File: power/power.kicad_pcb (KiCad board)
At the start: 0 parts

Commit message: mainboard v0.3 + power WIP
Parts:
- added BT1: Cell 1, Connector_PinHeader_2.54mm:PinHeader_1x02_P2.54mm_Vertical, F.Cu at (70.8, 190.2)
- added BT2: Cell 2, Connector_PinHeader_2.54mm:PinHeader_1x02_P2.54mm_Vertical, F.Cu at (70.8, 196.4)
- added BT3: Cell 3, Connector_PinHeader_2.54mm:PinHeader_1x02_P2.54mm_Vertical, F.Cu at (70.8, 202.6)
- added BT4: Cell 4, Connector_PinHeader_2.54mm:PinHeader_1x02_P2.54mm_Vertical, F.Cu at (70.8, 208.8)
- added C1: 1uF, Capacitor_SMD:C_0603_1608Metric, F.Cu at (187.0, 118.2)
- added C10: 100nF, Capacitor_SMD:C_0603_1608Metric, F.Cu at (184.8, 107.3)
- added C11: 1uF, Capacitor_SMD:C_0603_1608Metric, F.Cu at (57.8, 164.6)
- added C12: 1uF, Capacitor_SMD:C_0603_1608Metric, F.Cu at (57.8, 167.1)
- added C13: 1uF, Capacitor_SMD:C_0603_1608Metric, F.Cu at (75.1, 191.7)
- added C14: 1uF, Capacitor_SMD:C_0603_1608Metric, F.Cu at (75.2, 196.6)
- added C15: 1uF, Capacitor_SMD:C_0603_1608Metric, F.Cu at (75.1, 202.0)
- added C16: 1uF, Capacitor_SMD:C_0603_1608Metric, F.Cu at (75.2, 208.1)
- added C17: 1uF, Capacitor_SMD:C_0603_1608Metric, F.Cu at (75.3, 211.7)
- added C18: 0.1uF, Capacitor_SMD:C_0603_1608Metric, F.Cu at (100.0, 187.0)
- added C19: 0.1uF, Capacitor_SMD:C_0603_1608Metric, F.Cu at (100.0, 189.6)
- added C2: 10uF, Capacitor_SMD:C_0603_1608Metric, F.Cu at (36.5, 64.1)
- added C20: 0.1uF, Capacitor_SMD:C_0603_1608Metric, F.Cu at (100.0, 192.1)
- added C21: 0.1uF, Capacitor_SMD:C_0603_1608Metric, F.Cu at (100.0, 194.6)
- added C22: 0.1uF, Capacitor_SMD:C_0603_1608Metric, F.Cu at (104.0, 187.0)
- added C23: 1uF, Capacitor_SMD:C_0603_1608Metric, F.Cu at (73.6, 208.1)
- added C24: 10uF, Capacitor_SMD:C_0603_1608Metric, F.Cu at (69.8, 186.7)
- added C25: 10uF, Capacitor_SMD:C_0603_1608Metric, F.Cu at (71.4, 186.7)
- added C26: 100nF, Capacitor_SMD:C_0603_1608Metric, F.Cu at (73.1, 186.7)
- added C27: 1uF, Capacitor_SMD:C_0603_1608Metric, F.Cu at (174.4, 112.8)
- added C28: 10uF, Capacitor_SMD:C_0603_1608Metric, F.Cu at (181.6, 107.4)
- added C29: 10uF, Capacitor_SMD:C_0603_1608Metric, F.Cu at (186.4, 107.3)
- added C3: 10uF, Capacitor_SMD:C_0603_1608Metric, F.Cu at (36.5, 66.6)
- added C30: 10uF, Capacitor_SMD:C_0603_1608Metric, F.Cu at (182.8, 110.6)
- added C31: 10uF, Capacitor_SMD:C_0603_1608Metric, F.Cu at (181.1, 112.8)
- added C32: 10uF, Capacitor_SMD:C_0603_1608Metric, F.Cu at (179.4, 112.8)
- added C33: 10uF, Capacitor_SMD:C_0603_1608Metric, F.Cu at (177.8, 112.8)
- added C34: 33nF, Capacitor_SMD:C_0603_1608Metric, F.Cu at (178.5, 105.4)
- added C35: 33nF, Capacitor_SMD:C_0603_1608Metric, F.Cu at (172.9, 105.4)
- added C36: 470nF, Capacitor_SMD:C_0603_1608Metric, F.Cu at (162.8, 107.6)
- added C37: 10nF, Capacitor_SMD:C_0603_1608Metric, F.Cu at (172.7, 112.8)
- added C38: 47nF, Capacitor_SMD:C_0603_1608Metric, F.Cu at (161.9, 110.5)
- added C39: 47nF, Capacitor_SMD:C_0603_1608Metric, F.Cu at (155.6, 110.5)
- added C4: 10uF, Capacitor_SMD:C_0603_1608Metric, F.Cu at (36.5, 69.1)
- added C40: 10uF, Capacitor_SMD:C_0603_1608Metric, F.Cu at (145.2, 107.6)
- added C41: 10uF, Capacitor_SMD:C_0603_1608Metric, F.Cu at (143.4, 107.6)
- added C42: 10uF, Capacitor_SMD:C_0603_1608Metric, F.Cu at (141.6, 107.6)
- added C43: 10uF, Capacitor_SMD:C_0603_1608Metric, F.Cu at (141.8, 104.4)
- added C44: 10uF, Capacitor_SMD:C_0603_1608Metric, F.Cu at (143.5, 104.4)
- added C45: 10uF, Capacitor_SMD:C_0603_1608Metric, F.Cu at (145.3, 104.4)
- added C46: 1uF, Capacitor_SMD:C_0603_1608Metric, F.Cu at (145.2, 95.2)
- added C47: 2.2uF, Capacitor_SMD:C_0603_1608Metric, F.Cu at (158.8, 110.5)
- added C48: 1uF, Capacitor_SMD:C_0603_1608Metric, F.Cu at (163.8, 105.0)
- added C49: 680pF, Capacitor_SMD:C_0603_1608Metric, F.Cu at (153.5, 99.2)
- added C5: 0.1uF, Capacitor_SMD:C_0603_1608Metric, F.Cu at (36.5, 71.6)
- added C50: 15pF, Capacitor_SMD:C_0603_1608Metric, F.Cu at (154.3, 101.6)
- added C51: 33pF, Capacitor_SMD:C_0603_1608Metric, F.Cu at (157.5, 101.5)
- added C52: 1800pF, Capacitor_SMD:C_0603_1608Metric, F.Cu at (156.7, 99.2)
- added C53: 100pF, Capacitor_SMD:C_0603_1608Metric, F.Cu at (163.9, 103.3)
- added C54: 100pF, Capacitor_SMD:C_0603_1608Metric, F.Cu at (164.7, 100.8)
- added C55: 0.1uF, Capacitor_SMD:C_0603_1608Metric, F.Cu at (142.0, 96.0)
- added C56: 10uF, Capacitor_SMD:C_0603_1608Metric, F.Cu at (126.4, 16.2)
- added C57: 0.1uF, Resistor_SMD:R_0603_1608Metric, F.Cu at (126.4, 18.7)
- added C6: 1uF, Capacitor_SMD:C_0603_1608Metric, F.Cu at (126.4, 11.2)
- added C7: 1uF, Capacitor_SMD:C_0603_1608Metric, F.Cu at (126.4, 13.7)
- added C8: 10uF, Capacitor_SMD:C_0603_1608Metric, F.Cu at (183.2, 107.4)
- added C9: 10uF, Capacitor_SMD:C_0603_1608Metric, F.Cu at (184.5, 110.5)
- added D1: MMSZ5248B, Diode_SMD:D_SOD-123, F.Cu at (100.9, 206.9)
- added D2: BAS316, Diode_SMD:D_SOD-323, F.Cu at (78.0, 182.2)
- added D3: SMBJ26A-13-F, Diode_SMD:D_SMB, F.Cu at (77.8, 186.0)
- added D4: LED1, LED_SMD:LED_0603_1608Metric, F.Cu at (121.8, 36.6)
- added D5: LED2, LED_SMD:LED_0603_1608Metric, F.Cu at (121.8, 39.2)
- added D6: LED3, LED_SMD:LED_0603_1608Metric, F.Cu at (121.8, 41.8)
- added D7: LED4, LED_SMD:LED_0603_1608Metric, F.Cu at (121.8, 44.4)
- added D8: LED5, LED_SMD:LED_0603_1608Metric, F.Cu at (121.8, 46.9)
- added J1: USB-C Power + USB2.0, Connector_USB:USB_C_Receptacle_HRO_TYPE-C-31-M-12, F.Cu at (196.9, 113.1)
- added J2: USB, FPC:FPC-SMD_6P-P0.50_XUNPU_FPC-05F-6PH20, F.Cu at (103.2, 130.6)
- added L1: MWSA0603S-100MT, Inductor_SMD:L_Sunlord_MWSA0603S, F.Cu at (43.4, 67.0)
- added L2: MWSA0603S-2R2MT, Inductor_SMD:L_Sunlord_MWSA0603S, F.Cu at (158.7, 115.2)
- added Q1: SI7617DN-T1-GE3, Package_SO:Vishay_PowerPAK_1212-8_Single, F.Cu at (187.9, 110.9)
- added Q2: CSD18534Q5A, Package_TO_SOT_SMD:TDSON-8-1, F.Cu at (111.7, 199.2)
- added Q3: CSD18534Q5A, Package_TO_SOT_SMD:TDSON-8-1, F.Cu at (111.7, 205.9)
- added Q4: CSD18534Q5A, Package_TO_SOT_SMD:TDSON-8-1, F.Cu at (168.6, 108.7)
- added Q5: CSD18534Q5A, Package_TO_SOT_SMD:TDSON-8-1, F.Cu at (168.1, 115.5)
- added Q6: CSD18534Q5A, Package_TO_SOT_SMD:TDSON-8-1, F.Cu at (149.3, 115.6)
- added Q7: CSD18534Q5A, Package_TO_SOT_SMD:TDSON-8-1, F.Cu at (149.7, 108.5)
- added Q8: CSD18534Q5A, Package_TO_SOT_SMD:TDSON-8-1, F.Cu at (149.7, 100.8)
- added R1: 1M, Resistor_SMD:R_0603_1608Metric, F.Cu at (193.1, 106.8)
- added R10: 33R, Resistor_SMD:R_0603_1608Metric, F.Cu at (74.3, 189.3)
- added R11: 7.5k, Resistor_SMD:R_0603_1608Metric, F.Cu at (36.5, 74.1)
- added R12: 24k, Resistor_SMD:R_0603_1608Metric, F.Cu at (36.5, 76.7)
- added R13: 56k, Resistor_SMD:R_0603_1608Metric, F.Cu at (36.5, 79.2)
- added R14: 10k, Resistor_SMD:R_0603_1608Metric, F.Cu at (36.5, 81.7)
- added R15: 33R, Resistor_SMD:R_0603_1608Metric, F.Cu at (74.4, 194.2)
- added R16: 33R, Resistor_SMD:R_0603_1608Metric, F.Cu at (74.4, 199.4)
- added R17: 33R, Resistor_SMD:R_0603_1608Metric, F.Cu at (74.4, 204.9)
- added R18: 33R, Resistor_SMD:R_0603_1608Metric, F.Cu at (73.7, 211.7)
- added R19: 1k, Resistor_SMD:R_0603_1608Metric, F.Cu at (65.8, 172.2)
- added R2: 10R, Resistor_SMD:R_0603_1608Metric, F.Cu at (190.1, 118.2)
- added R20: 15mΩ SHUNT RLP25FEER015, Resistor_SMD:R_Shunt_Vishay_WSK2512_6332Metric_T1.19mm, F.Cu at (115.0, 188.2)
- added R21: 100R, Resistor_SMD:R_0603_1608Metric, F.Cu at (104.0, 189.6)
- added R22: 100R, Resistor_SMD:R_0603_1608Metric, F.Cu at (104.0, 192.1)
- added R23: 5.1k, Resistor_SMD:R_0603_1608Metric, F.Cu at (65.8, 179.7)
- added R24: 5.1k, Resistor_SMD:R_0603_1608Metric, F.Cu at (65.8, 182.2)
- added R25: 10M, Resistor_SMD:R_0603_1608Metric, F.Cu at (104.0, 194.6)
- added R26: 3M, Resistor_SMD:R_0603_1608Metric, F.Cu at (108.0, 187.0)
- added R27: 1M, Resistor_SMD:R_0603_1608Metric, F.Cu at (69.8, 167.1)
- added R28: 470k, Resistor_SMD:R_0603_1608Metric, F.Cu at (108.0, 189.6)
- added R29: 100k, Resistor_SMD:R_0603_1608Metric, F.Cu at (108.0, 192.1)
- added R3: 5.1k, Resistor_SMD:R_0603_1608Metric, F.Cu at (183.7, 118.2)
- added R30: 10k, Resistor_SMD:R_0603_1608Metric, F.Cu at (108.0, 194.6)
- added R31: 10k, Resistor_SMD:R_0603_1608Metric, F.Cu at (69.8, 177.2)
- added R32: 10k, Resistor_SMD:R_0603_1608Metric, F.Cu at (69.8, 179.7)
- added R33: 2.2R, Resistor_SMD:R_0603_1608Metric, F.Cu at (176.1, 112.8)
- added R34: 10mΩ SHUNT FMF25FPJR010-LH, Resistor_SMD:R_Shunt_Vishay_WSK2512_6332Metric_T1.19mm, F.Cu at (176.3, 109.1)
- added R35: 5.1R, Resistor_SMD:R_0603_1608Metric, F.Cu at (176.8, 105.4)
- added R36: 5.1R, Resistor_SMD:R_0603_1608Metric, F.Cu at (174.7, 105.4)
- added R37: 10mΩ SHUNT FMF25FPJR010-LH, Resistor_SMD:R_Shunt_Vishay_WSK2512_6332Metric_T1.19mm, F.Cu at (141.7, 99.0)
- added R38: 10R, Resistor_SMD:R_0603_1608Metric, F.Cu at (143.0, 93.3)
- added R39: 10R, Resistor_SMD:R_0603_1608Metric, F.Cu at (141.2, 93.3)
- added R4: 49.9k, Resistor_SMD:R_0603_1608Metric, F.Cu at (189.8, 108.2)
- added R40: 130k, Resistor_SMD:R_0603_1608Metric, F.Cu at (154.4, 103.5)
- added R41: 470k, Resistor_SMD:R_0603_1608Metric, F.Cu at (154.4, 105.1)
- added R42: 390k, Resistor_SMD:R_0603_1608Metric, F.Cu at (166.4, 102.8)
- added R43: 220k, Resistor_SMD:R_0603_1608Metric, F.Cu at (168.9, 103.5)
- added R44: 10R, Resistor_SMD:R_0603_1608Metric, F.Cu at (164.7, 107.5)
- added R45: 2M, Resistor_SMD:R_0603_1608Metric, F.Cu at (160.7, 101.5)
- added R46: 300k, Resistor_SMD:R_0603_1608Metric, F.Cu at (160.7, 99.8)
- added R47: 10k, Resistor_SMD:R_0603_1608Metric, F.Cu at (146.2, 157.9)
- added R48: 10k, Resistor_SMD:R_0603_1608Metric, F.Cu at (150.7, 153.2)
- added R49: 10k, Resistor_SMD:R_0603_1608Metric, F.Cu at (150.7, 155.7)
- added R5: DNP, Resistor_SMD:R_0603_1608Metric, F.Cu at (183.7, 116.4)
- added R50: 10k, Resistor_SMD:R_0603_1608Metric, F.Cu at (117.7, 36.5)
- added R51: 10k, Resistor_SMD:R_0603_1608Metric, F.Cu at (117.7, 39.0)
- added R52: 10k, Resistor_SMD:R_0603_1608Metric, F.Cu at (155.1, 99.2)
- added R53: 40.2k, Resistor_SMD:R_0603_1608Metric, F.Cu at (158.3, 99.2)
- added R54: 200R, Resistor_SMD:R_0603_1608Metric, F.Cu at (150.7, 158.2)
- added R55: 110k, Resistor_SMD:R_0603_1608Metric, F.Cu at (163.1, 100.8)
- added R56: 27k, Resistor_SMD:R_0603_1608Metric, F.Cu at (163.9, 98.5)
- added R57: 1k, Resistor_SMD:R_0603_1608Metric, F.Cu at (126.4, 21.2)
- added R58: 10k, Resistor_SMD:R_0603_1608Metric, F.Cu at (126.4, 23.8)
- added R59: 10k, Resistor_SMD:R_0603_1608Metric, F.Cu at (117.7, 41.6)
- added R6: DNP, Resistor_SMD:R_0603_1608Metric, F.Cu at (183.7, 113.0)
- added R60: 10k, Resistor_SMD:R_0603_1608Metric, F.Cu at (117.7, 44.1)
- added R61: 10k, Resistor_SMD:R_0603_1608Metric, F.Cu at (117.7, 46.6)
- added R62: 10k, Resistor_SMD:R_0603_1608Metric, F.Cu at (117.7, 49.1)
- added R63: 10k, Resistor_SMD:R_0603_1608Metric, F.Cu at (117.7, 51.6)
- added R7: 0R, Resistor_SMD:R_0603_1608Metric, F.Cu at (183.7, 114.7)
- added R8: 2.2k, Resistor_SMD:R_0603_1608Metric, F.Cu at (72.1, 91.3)
- added R9: 50mΩ SHUNT LR122WF500MT4E, Resistor_SMD:R_Shunt_Vishay_WSK2512_6332Metric_T1.19mm, F.Cu at (69.4, 87.6)
- added SW1: RST, Button_Switch_SMD:SW_Push_1P1T_XKB_TS-1187A, F.Cu at (82.2, 49.6)
- added SW2: BOOT, Button_Switch_SMD:SW_Push_1P1T_XKB_TS-1187A, F.Cu at (82.2, 56.2)
- added TH1: 103AT 10k, Connector_PinHeader_2.54mm:PinHeader_1x02_P2.54mm_Vertical, F.Cu at (76.7, 158.5)
- added TP1: CCFG, TestPoint:TestPoint_Pad_2.0x2.0mm, F.Cu at (94.3, 167.8)
- added TP2: CMPIN, TestPoint:TestPoint_Pad_2.0x2.0mm, F.Cu at (160.7, 97.5)
- added TP3: CMPOUT, TestPoint:TestPoint_Pad_2.0x2.0mm, F.Cu at (167.3, 99.3)
- added U1: HUSB238, HUSB238:DFN-10_L3.0-W3.0-P0.50-BL-EP2.5, F.Cu at (188.0, 115.3)
- added U2: LTC2943, LTC2943:DFN-8_DD_LIT, F.Cu at (67.4, 92.4)
- added U3: BQ7791501PWR, BQ77915:SOP65P640X120-24N, F.Cu at (82.4, 200.3)
- added U4: BQ25713RSNR, BQ25713:RSN0032B, F.Cu at (159.0, 106.0)
- added U5: ESP32-S3-MINI-1, RF_Module:ESP32-S2-MINI-1, F.Cu at (101.2, 35.2)
- added U6: TVS2200DRV, Package_SON:WSON-6-1EP_2x2mm_P0.65mm_EP1x1.6mm, F.Cu at (188.6, 105.8)
- added U7: TPS560200, Package_TO_SOT_SMD:SOT-23-5, F.Cu at (41.0, 73.5)
- added U8: CP2102N-Axx-xQFN28, Package_DFN_QFN:QFN-28-1EP_5x5mm_P0.5mm_EP3.35x3.35mm, F.Cu at (90.1, 49.9)
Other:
- copper layers 0 -> 2

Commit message: power v0.1 layout done
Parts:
- L1: value MWSA0603S-100MT -> FTC252012S100MBCA; footprint Inductor_SMD:L_Sunlord_MWSA0603S -> Inductor_SMD:L_1008_2520Metric
- moved C2 149.4 mm to (166.8, 137.3), turned to 180 degrees
- moved C3 146.5 mm to (168.7, 129.5), turned to 180 degrees
- moved R12 143.1 mm to (168.8, 131.2)
- moved C4 142.3 mm to (165.3, 129.5), turned to 180 degrees
- moved L1 142.3 mm to (168.8, 134.3), turned to 90 degrees
- moved C5 141.9 mm to (165.3, 131.2), turned to 180 degrees
- moved C56 140.6 mm to (198.9, 136.7), turned to 90 degrees
- moved R14 138.8 mm to (163.6, 137.4), turned to 180 degrees
- moved R11 138.7 mm to (162.7, 131.7), turned to -90 degrees
- moved U7 138.3 mm to (165.3, 134.2), turned to 90 degrees
- moved R13 137.9 mm to (162.7, 134.9), turned to 90 degrees
- moved C57 137.6 mm to (197.2, 136.7), turned to 90 degrees
- moved R8 132.1 mm to (198.1, 131.1)
- moved U5 131.4 mm to (188.2, 133.6), turned to 180 degrees
- moved C7 131.3 mm to (179.4, 133.8), turned to -90 degrees
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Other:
- board outline added: 64 x 47.2 mm

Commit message: power sub 50 routes
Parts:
- added J3: BATTERY OUT, Connector_Molex:Molex_PicoBlade_53261-1071_1x10-1MP_P1.25mm_Horizontal, F.Cu at (138.9, 107.2)
- added J4: BACKUP, Connector_PinHeader_2.54mm:PinHeader_1x02_P2.54mm_Vertical, F.Cu at (175.7, 120.4)
- moved R9 28.0 mm to (144.7, 104.8)
- moved TH1 27.5 mm to (171.5, 126.9), turned to 180 degrees
- moved U2 27.2 mm to (148.5, 106.5)
- moved J2 14.4 mm to (167.1, 123.8)
- moved C24 9.48 mm to (145.9, 118.6), turned to -90 degrees
- moved C50 9.21 mm to (163.5, 101.1)
- moved R52 9.20 mm to (164.3, 98.8)
- moved C49 9.20 mm to (162.7, 98.8)
- moved C46 9.20 mm to (155.2, 98.8)
- moved R38 9.20 mm to (152.8, 97.9)
- moved C31 9.20 mm to (190.3, 110.3)
- moved C37 9.20 mm to (181.9, 110.3)
- moved C40 9.20 mm to (154.8, 109.8)
- moved C41 9.20 mm to (153.0, 109.8)
- moved C42 9.20 mm to (151.2, 109.8)
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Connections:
- C18 pad 1: /SRN -> /BMS_SRN
- C18 pad 2: /SRP -> /BMS_SRP
- C19 pad 1: /SRP -> /BMS_SRP
- C20 pad 1: /SRN -> /BMS_SRN
- R21 pad 2: /SRN -> /BMS_SRN
- R22 pad 2: /SRP -> /BMS_SRP
- U3 pad 10: /SRP -> /BMS_SRP
- U3 pad 11: /SRN -> /BMS_SRN
- U5 pad 21: unconnected-(U5-IO17-Pad21) -> Net-(J4-Pin_2)
- U5 pad 22: unconnected-(U5-IO18-Pad22) -> Net-(J4-Pin_1)
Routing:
- net Net-(J1-VBUS-PadA4): track 0.00 -> 34.6 mm
- net +3.3V: track 0.00 -> 33.5 mm
- net Net-(U3-TS): track 0.00 -> 30.4 mm, vias 0 -> 2
- net /IO0: track 0.00 -> 27.2 mm
- net /SW2: track 0.00 -> 25.8 mm
- net Net-(J1-SHIELD): track 0.00 -> 24.8 mm
- net /SRN: track 0.00 -> 22.7 mm, vias 0 -> 2
- net /SW1: track 0.00 -> 22.2 mm
- net Net-(C21-Pad1): track 0.00 -> 19.4 mm, vias 0 -> 2
- net Net-(U3-CHG): track 0.00 -> 19.3 mm, vias 0 -> 2
- net /PACK+: track 0.00 -> 17.9 mm
- net /LODRV1: track 0.00 -> 17.3 mm, vias 0 -> 2
- net Net-(U8-~{RST}): track 0.00 -> 17.3 mm, vias 0 -> 2
- net /VC4: track 0.00 -> 16.8 mm, vias 0 -> 2
- net /EN: track 0.00 -> 16.6 mm
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- added copper zone on In1.Cu, net +3.3V
- added copper zone on In2.Cu, net +3.3V
- added copper zone on F.Cu, net /VBUS
- added copper zone on F.Cu, net /VSYS
- added copper zone on In1.Cu, net /VSYS
- added copper zone on B.Cu, net GND
- added copper zone on F.Cu, net GND
- added copper zone on In1.Cu, net GND
- added copper zone on In2.Cu, net GND
- added copper zone on B.Cu, net GNDPWR
- added copper zone on F.Cu, net GNDPWR
- added copper zone on In1.Cu, net GNDPWR
- added copper zone on In2.Cu, net GNDPWR
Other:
- board size 64 x 47.2 mm -> 64 x 45.4 mm
- copper layers 2 -> 4

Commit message: routing complete
routing complete
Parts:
- moved R43 1.56 mm to (178.0, 102.0)
- moved R45 1.15 mm to (169.9, 100.4)
- moved R46 1.05 mm to (169.9, 98.8)
- moved R44 0.83 mm to (174.3, 108.3)
- moved C36 0.73 mm to (172.1, 108.3)
- moved R35 0.35 mm to (185.8, 103.2)
- moved C34 0.32 mm to (187.6, 103.2)
- moved C30 0.26 mm to (189.7, 102.9)
- moved C28 0.19 mm to (187.0, 99.6)
- moved C8 0.19 mm to (188.6, 99.6)
- moved C9 0.15 mm to (191.3, 102.9)
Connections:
- U4 pad V: (no net) -> GND
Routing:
- net /SCL: track 3.20 -> 87.8 mm, vias 0 -> 4
- net /SDA: track 2.61 -> 85.2 mm, vias 0 -> 4
- net /~{ALCC}: track 2.37 -> 72.1 mm, vias 0 -> 4
- net /PRES: track 5.19 -> 71.3 mm, vias 0 -> 2
- net /CBI: track 2.74 -> 58.5 mm, vias 0 -> 2
- net /CMPOUT: track 6.58 -> 57.1 mm, vias 0 -> 5
- net /PROCHOT_N: track 2.02 -> 51.9 mm, vias 0 -> 4
- net /IBAT: track 3.10 -> 52.1 mm, vias 0 -> 3
- net /EN_OTG: track 2.64 -> 45.3 mm, vias 0 -> 4
- net /IADPT: track 5.83 -> 48.1 mm, vias 2 -> 4
- net +3.3V: track 33.5 -> 75.3 mm, vias 0 -> 4
- net /CHRG_OK: track 2.29 -> 43.9 mm, vias 0 -> 4
- net VDD: track 16.0 -> 52.4 mm, vias 0 -> 2
- net GNDPWR: track 7.39 -> 36.0 mm, vias 0 -> 10
- net /VDDA: track 9.90 -> 37.5 mm, vias 0 -> 4
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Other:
- outline, holes or cut-outs redrawn
- board text added: "0"
- board text added: "anyon_e"
- board text added: "byran '25"

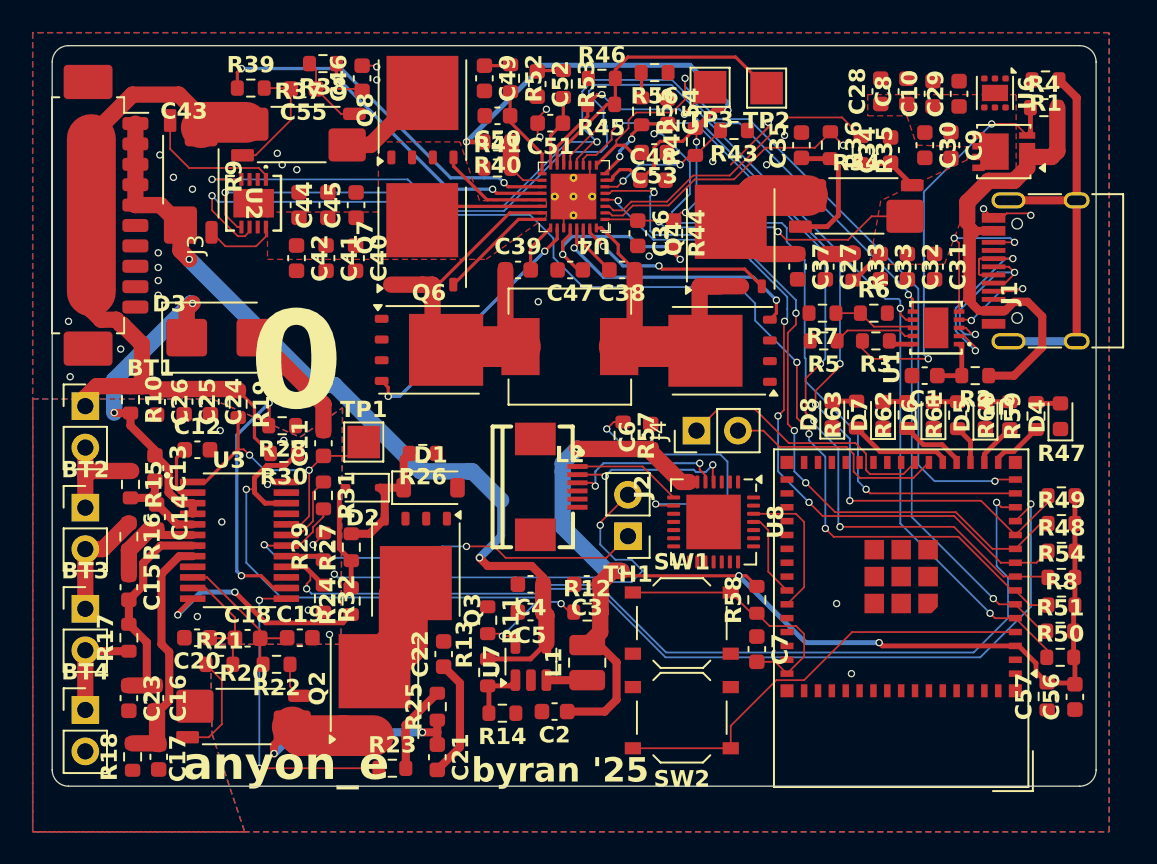
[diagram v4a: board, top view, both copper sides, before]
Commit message: silkscreening power
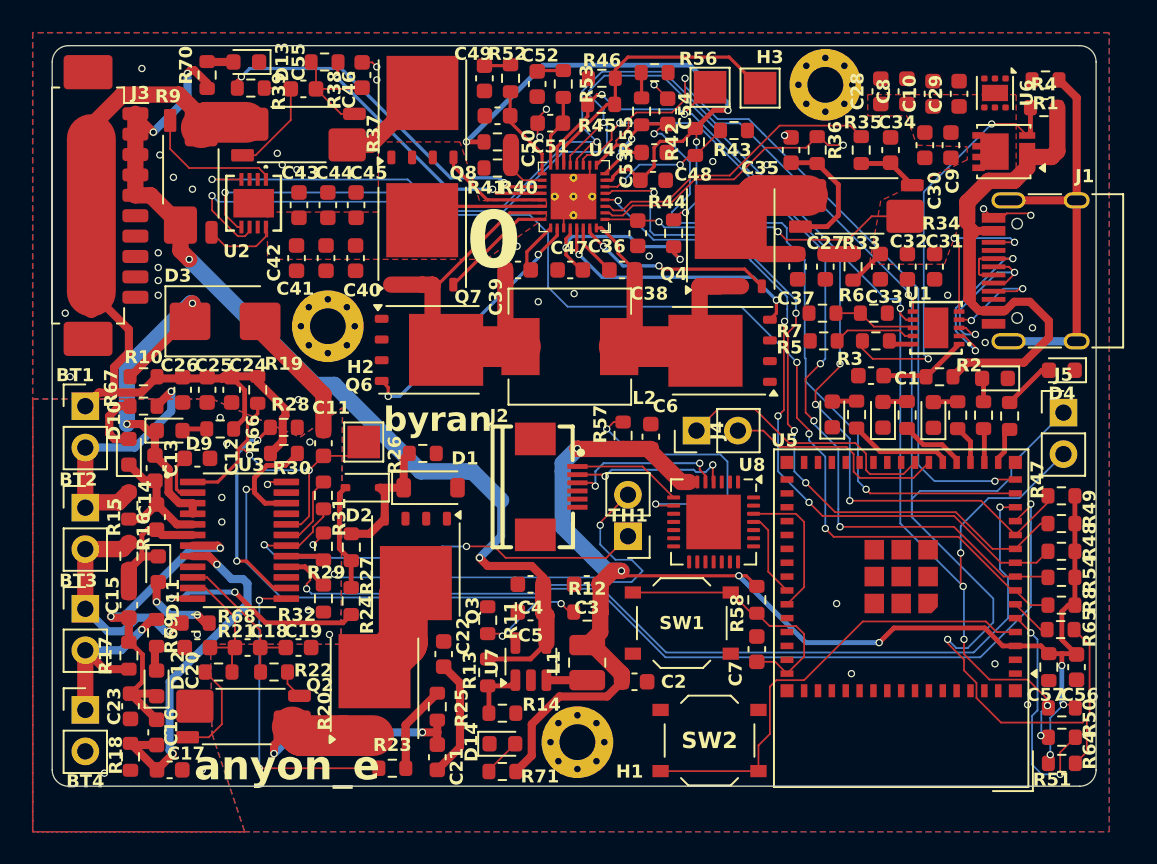
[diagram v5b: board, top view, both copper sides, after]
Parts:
- added D10: C3 LED, LED_SMD:LED_0603_1608Metric, F.Cu at (140.9, 121.7)
- added D11: C2 LED, LED_SMD:LED_0603_1608Metric, F.Cu at (142.7, 128.9)
- added D12: C1 LED, LED_SMD:LED_0603_1608Metric, F.Cu at (142.6, 135.9)
- added D13: VDD LED, LED_SMD:LED_0603_1608Metric, F.Cu at (148.1, 97.8)
- added D14: +3.3V LED, LED_SMD:LED_0603_1608Metric, F.Cu at (163.8, 139.6)
- added D9: C4 LED, LED_SMD:LED_0603_1608Metric, F.Cu at (143.4, 120.4)
- added H1: M2, MountingHole:MountingHole_2.2mm_M2_Pad_Via, F.Cu at (168.4, 139.5)
- added H2: M2, MountingHole:MountingHole_2.2mm_M2_Pad_Via, F.Cu at (153.1, 114.0)
- added H3: M2, MountingHole:MountingHole_2.2mm_M2_Pad_Via, F.Cu at (183.6, 99.2)
- added J5: I2C, Connector_PinHeader_2.54mm:PinHeader_1x02_P2.54mm_Vertical, F.Cu at (198.2, 119.3)
- added R64: 0R, Resistor_SMD:R_0603_1608Metric, F.Cu at (198.1, 139.2)
- added R65: 0R, Resistor_SMD:R_0603_1608Metric, F.Cu at (198.0, 132.6)
- added R66: 1k, Resistor_SMD:R_0603_1608Metric, F.Cu at (146.5, 120.3)
- added R67: 1k, Resistor_SMD:R_0603_1608Metric, F.Cu at (141.8, 118.9)
- added R68: 1k, Resistor_SMD:R_0603_1608Metric, F.Cu at (145.0, 132.2)
- added R69: 1k, Resistor_SMD:R_0603_1608Metric, F.Cu at (142.6, 132.8)
- added R70: 1k, Resistor_SMD:R_0603_1608Metric, F.Cu at (145.7, 98.6)
- added R71: 1k, Resistor_SMD:R_0603_1608Metric, F.Cu at (163.8, 141.3)
- moved R51 8.10 mm to (198.1, 140.8), turned to 180 degrees
- moved C2 5.23 mm to (171.9, 135.8), turned to 0 degrees
- moved C1 3.29 mm to (186.4, 117.0)
- moved R50 3.10 mm to (198.1, 137.4)
- moved D4 2.82 mm to (198.1, 116.7), turned to 180 degrees
- moved D5 2.34 mm to (194.0, 117.2), turned to 180 degrees
- moved SW2 2.20 mm to (176.5, 139.4)
- moved R2 2.19 mm to (190.6, 117.1)
- moved C16 2.10 mm to (142.6, 138.9)
- moved C56 1.83 mm to (199.0, 134.9)
- moved C57 1.80 mm to (197.3, 134.9)
- moved C26 1.77 mm to (144.2, 117.9)
- moved R59 1.61 mm to (194.9, 119.5)
- moved R60 1.61 mm to (193.3, 119.5)
- moved R10 1.61 mm to (141.8, 117.1), turned to 180 degrees
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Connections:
- net /PACK+ renamed /C4
- net Net-(BT1--) renamed /C3
- net Net-(BT2--) renamed /C2
- net Net-(BT3--) renamed /C1
- U5 pad 5: /SCL -> Net-(U5-IO1)
- U5 pad 6: /SDA -> Net-(U5-IO2)
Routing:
- net /SDA: track 85.2 -> 120.4 mm
- net /SCL: track 87.8 -> 106.7 mm, vias 4 -> 8
- net Net-(U5-IO1): track 0.00 -> 14.4 mm, vias 0 -> 2
- net +3.3V: track 75.3 -> 87.6 mm, vias 4 -> 7
- net /C3: track 6.64 -> 15.4 mm, vias 0 -> 1
- net VDD: track 52.4 -> 60.7 mm, vias 2 -> 4
- net /C4: track 43.9 -> 51.9 mm
- net /VC1: track 13.4 -> 20.6 mm, vias 0 -> 2
- net /C2: track 6.99 -> 13.9 mm, vias 0 -> 1
- net /VC0: track 15.1 -> 21.9 mm, vias 0 -> 2
- net /C1: track 6.35 -> 12.0 mm, vias 0 -> 1
- net Net-(D11-A): track 0.00 -> 5.02 mm, vias 0 -> 2
- net /IBAT: track 52.1 -> 47.7 mm, vias 3 -> 2
- net Net-(D10-A): track 0.00 -> 3.95 mm
- net /VC2: track 6.07 -> 9.38 mm
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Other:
- board text added: "@TODO: balancing & power LEDs"
- board text added: "ATTEMPT THE IMPOSSIBLE."
- board text added: "byran"
- board text removed: "byran '25"

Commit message: powertrain pcb v0.1 complete
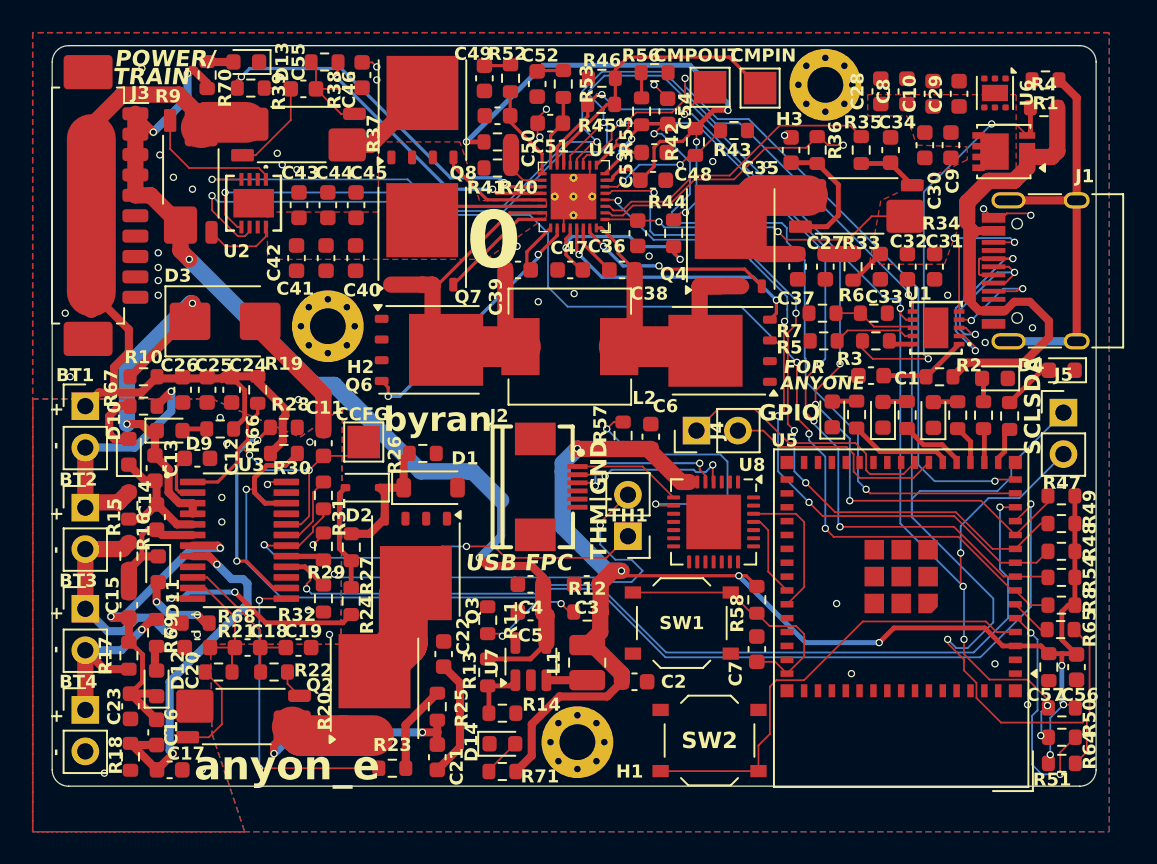
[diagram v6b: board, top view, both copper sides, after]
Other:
- board text added: "+ -"
- board text added: "ANYONE"
- board text added: "BYRAN HUANG '25"
- board text added: "CCFG"
- board text added: "CMPIN"
- board text added: "CMPOUT"
- board text added: "FOR __"
- board text added: "GPIO"
- board text added: "IN YOUR HANDS"
- board text added: "PHILLIPS EXETER ACADEMY"
- board text added: "POWER TRAIN V0.1"
- board text added: "POWER/"
- board text added: "SCLSDA"
- board text added: "THM|GND"
- board text added: "TRAIN"
- board text added: "USB FPC"
- board text removed: "@TODO: balancing & power LEDs"

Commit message: final tapeout
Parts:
- C57: footprint Resistor_SMD:R_0603_1608Metric -> Capacitor_SMD:C_0603_1608Metric
- J3: footprint Connector_Molex:Molex_PicoBlade_53261-1071_1x10-1MP_P1.25mm_Horizontal -> Connector_Molex:Molex_PicoBlade_53048-1010_1x10_P1.25mm_Horizontal
- moved J3 5.63 mm to (140.5, 101.2)
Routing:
- net /C4: track 51.9 -> 50.2 mm
- net Net-(U4-ACN): track 17.7 -> 16.2 mm, vias 1 -> 0
- net VDD: track 60.7 -> 62.1 mm
- net GND: vias 35 -> 34
- removed copper zone on In1.Cu, net +3.3V
- removed copper zone on In2.Cu, net +3.3V
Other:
- board text added: "POWER USB"
